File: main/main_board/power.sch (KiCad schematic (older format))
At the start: 28 parts, among them J1 Conn_02x08_Odd_Even, U3 MCP1755S-3302E/DB, U4 MCP1755S-3302E/DB, U7 MCP1755S-5002E/DB

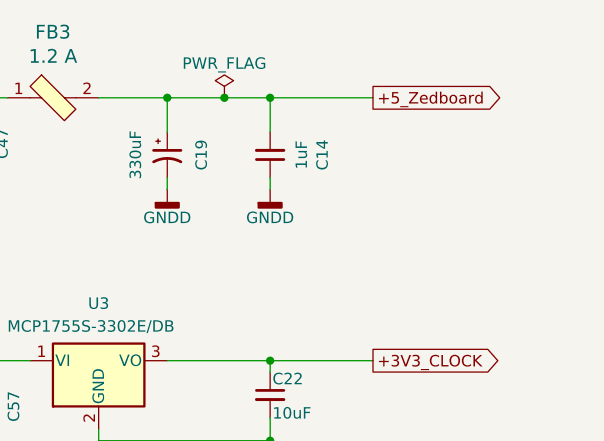
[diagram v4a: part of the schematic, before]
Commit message: Mostly work on main board layout. Aligned things on mm grid for easier routing, moved things around to create routing area. Neatened up component groups onto the grid. Parts of the routing plan are now drawn on the PCB.  See also notebook.txt. Reduced pad size of the PCIE connector, tweaked design rule clearances. Minor schematic tweaks.
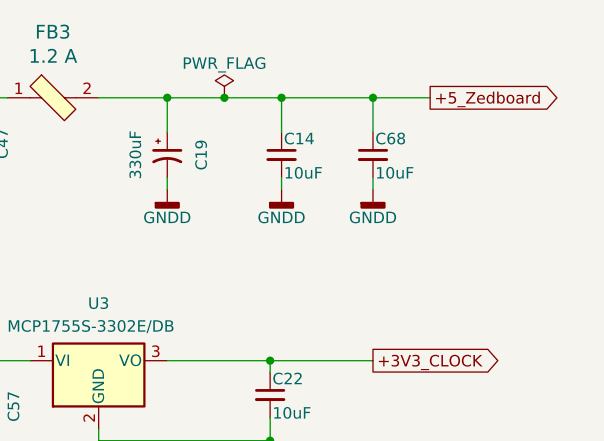
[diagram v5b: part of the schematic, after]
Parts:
- added C68: 10uF, Capacitor_SMD:C_0603_1608Metric, symbol Device:C_Small
- C14: value 1uF -> 10uF; footprint Capacitor_SMD:C_0805_2012Metric -> Capacitor_SMD:C_0603_1608Metric; DK line 27 -> 29; Description CAP CER 1UF 16V X7R 0805 -> CAP CER 10UF 6.3V X5R 0603; Digikey 1276-6471-1-ND -> 478-5318-1-ND; MPN CL21B105KOFNNNG -> 06036D106MAT2A; Manufacturer Samsung Electro-Mechanics -> (none)
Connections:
- net +5_Zedboard: now also C14.1, C68.1; no longer C14.2
- net GND: now also C14.2, C68.2; no longer C14.1
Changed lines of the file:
@@
 	1    0    0    -1
 $EndComp
-Text GLabel 9950 1200 2    50   Output ~ 0
+Text GLabel 10200 1200 2    50   Output ~ 0
 +5_Zedboard
 $Comp
@@
 $EndComp
 Wire Wire Line
-	9500 1200 9500 1350
-Wire Wire Line
-	9500 1550 9500 1600
+	9550 1200 9550 1350
+Wire Wire Line
+	9550 1550 9550 1600
 $Comp
 L power:GNDD #PWR011
 U 1 1 5ECF1209
-P 9500 1600
-F 0 "#PWR011" H 9500 1350 50  0001 C CNN
-F 1 "GNDD" H 9500 1475 50  0000 C CNN
-F 2 "" H 9500 1600 50  0001 C CNN
-F 3 "" H 9500 1600 50  0001 C CNN
-	1    9500 1600
-	1    0    0    -1
-$EndComp
-$Comp
-L Device:C_Small C?
-U 1 1 5ECEF1CE
-P 9500 1450
-AR Path="/5DFF6C0D/5ECEF1CE" Ref="C?"  Part="1"
-AR Path="/5E1D6729/5E1DA2AA/5ECEF1CE" Ref="C?"  Part="1"
-AR Path="/5E2EB92B/5ECEF1CE" Ref="C?"  Part="1"
-AR Path="/5E624B3C/5E2EB92B/5ECEF1CE" Ref="C?"  Part="1"
-AR Path="/5EBEDCCA/5ECEF1CE" Ref="C?"  Part="1"
-AR Path="/5E525EB8/5ECEF1CE" Ref="C?"  Part="1"
-AR Path="/5E525FC9/5ECEF1CE" Ref="C14"  Part="1"
-F 0 "C14" V 9271 1450 50  0000 C CNN
-F 1 "1uF" V 9362 1450 50  0000 C CNN
-F 2 "Capacitor_SMD:C_0805_2012Metric" H 9500 1450 50  0001 C CNN
-F 3 "https://media.digikey.com/pdf/Data%20Sheets/Samsung%20PDFs/CL_Series_MLCC_ds.pdf" H 9500 1450 50  0001 C CNN
-F 4 "CAP CER 1UF 16V X7R 0805 " H 9500 1450 50  0001 C CNN "Description"
-F 5 "1276-6471-1-ND" H 9500 1450 50  0001 C CNN "Digikey"
-F 6 "CL21B105KOFNNNG" H 9500 1450 50  0001 C CNN "MPN"
-F 7 "27" H 9500 1450 50  0001 C CNN "DK line"
-F 8 "Samsung Electro-Mechanics" H 9500 1450 50  0001 C CNN "Manufacturer"
-	1    9500 1450
-	-1   0    0    1
+P 9550 1600
+F 0 "#PWR011" H 9550 1350 50  0001 C CNN
+F 1 "GNDD" H 9550 1475 50  0000 C CNN
+F 2 "" H 9550 1600 50  0001 C CNN
+F 3 "" H 9550 1600 50  0001 C CNN
+	1    9550 1600
+	1    0    0    -1
 $EndComp
 Text GLabel 2250 1450 2    50   Output ~ 0
@@
 Text GLabel 3450 5050 2    50   Output ~ 0
 -6V
-Connection ~ 9500 1200
-Wire Wire Line
-	9500 1200 9950 1200
 Wire Wire Line
 	7900 1200 8100 1200
@@
 $EndComp
 Connection ~ 9300 1200
-Wire Wire Line
-	9300 1200 9500 1200
 $Comp
 L power:GNDD #PWR0108
@@
 	3950 2000 3950 2050
 Connection ~ 3950 2050
+$Comp
+L Device:C_Small C?
+U 1 1 5F0D2030
+P 9550 1450
+AR Path="/5DFCF14D/5DA78AA2/5F0D2030" Ref="C?"  Part="1"
+AR Path="/5DFCF14D/5E295469/5F0D2030" Ref="C?"  Part="1"
+AR Path="/5E448095/5DA78AA2/5F0D2030" Ref="C?"  Part="1"
+AR Path="/5E45936E/5DA78AA2/5F0D2030" Ref="C?"  Part="1"
+AR Path="/5E525F2C/5E6427A0/5DA78AA2/5F0D2030" Ref="C?"  Part="1"
+AR Path="/5E624B3C/5DFCF14D/5DA78AA2/5F0D2030" Ref="C?"  Part="1"
+AR Path="/5E624B3C/5E448095/5DA78AA2/5F0D2030" Ref="C?"  Part="1"
+AR Path="/5E624B3C/5E45936E/5DA78AA2/5F0D2030" Ref="C?"  Part="1"
+AR Path="/5E525F2C/5F0D2030" Ref="C?"  Part="1"
+AR Path="/5E525FC9/5F0D2030" Ref="C14"  Part="1"
+F 0 "C14" H 9560 1520 50  0000 L CNN
+F 1 "10uF" H 9560 1370 50  0000 L CNN
+F 2 "Capacitor_SMD:C_0603_1608Metric" H 9550 1450 50  0001 C CNN
+F 3 "http://datasheets.avx.com/cx5r.pdf" H 9550 1450 50  0001 C CNN
+F 4 "CAP CER 10UF 6.3V X5R 0603" H 9550 1450 50  0001 C CNN "Description"
+F 5 "478-5318-1-ND" H 9550 1450 50  0001 C CNN "Digikey"
+F 6 "06036D106MAT2A" H 9550 1450 50  0001 C CNN "MPN"
+F 7 "29" H 9550 1450 50  0001 C CNN "DK line"
+	1    9550 1450
+	1    0    0    -1
+$EndComp
+Wire Wire Line
+	9950 1550 9950 1600
+$Comp
+L power:GNDD #PWR0125
+U 1 1 5F0DBAD8
+P 9950 1600
+F 0 "#PWR0125" H 9950 1350 50  0001 C CNN
+F 1 "GNDD" H 9950 1475 50  0000 C CNN
+F 2 "" H 9950 1600 50  0001 C CNN
+F 3 "" H 9950 1600 50  0001 C CNN
+	1    9950 1600
+	1    0    0    -1
+$EndComp
+$Comp
+L Device:C_Small C?
+U 1 1 5F0DBAE2
+P 9950 1450
+AR Path="/5DFCF14D/5DA78AA2/5F0DBAE2" Ref="C?"  Part="1"
+AR Path="/5DFCF14D/5E295469/5F0DBAE2" Ref="C?"  Part="1"
+AR Path="/5E448095/5DA78AA2/5F0DBAE2" Ref="C?"  Part="1"
+AR Path="/5E45936E/5DA78AA2/5F0DBAE2" Ref="C?"  Part="1"
+AR Path="/5E525F2C/5E6427A0/5DA78AA2/5F0DBAE2" Ref="C?"  Part="1"
+AR Path="/5E624B3C/5DFCF14D/5DA78AA2/5F0DBAE2" Ref="C?"  Part="1"
+AR Path="/5E624B3C/5E448095/5DA78AA2/5F0DBAE2" Ref="C?"  Part="1"
+AR Path="/5E624B3C/5E45936E/5DA78AA2/5F0DBAE2" Ref="C?"  Part="1"
+AR Path="/5E525F2C/5F0DBAE2" Ref="C?"  Part="1"
+AR Path="/5E525FC9/5F0DBAE2" Ref="C68"  Part="1"
+F 0 "C68" H 9960 1520 50  0000 L CNN
+F 1 "10uF" H 9960 1370 50  0000 L CNN
+F 2 "Capacitor_SMD:C_0603_1608Metric" H 9950 1450 50  0001 C CNN
+F 3 "http://datasheets.avx.com/cx5r.pdf" H 9950 1450 50  0001 C CNN
+F 4 "CAP CER 10UF 6.3V X5R 0603" H 9950 1450 50  0001 C CNN "Description"
+F 5 "478-5318-1-ND" H 9950 1450 50  0001 C CNN "Digikey"
+F 6 "06036D106MAT2A" H 9950 1450 50  0001 C CNN "MPN"
+F 7 "29" H 9950 1450 50  0001 C CNN "DK line"
+	1    9950 1450
+	1    0    0    -1
+$EndComp
+Connection ~ 9550 1200
+Wire Wire Line
+	9550 1200 9950 1200
+Wire Wire Line
+	9300 1200 9550 1200
+Wire Wire Line
+	9950 1350 9950 1200
+Connection ~ 9950 1200
+Wire Wire Line
+	9950 1200 10200 1200
 $EndSCHEMATC

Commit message: Various preparations for routing the main board. Cleaned up the BOM and reconciled it with the Digikey BOM, so lots of component attributes have changed. This involved pinning down some components which had been vague, especially ferrite beads and chip capacitors. 1uF capacitors have all been changed to 10uF. Changed CARDSEL lines to be buffered rather than filtered, since we had the unused buffers sitting there. Another pass on the Microzed pin mapping.  Brought out the DEBUG LVDS line, and tweaked orderings. Added RC filter and pullups on I2C and PROBE_CONFIG.  We might need level translators here to get >=3.3V Added mount holes for the low volt regulator daughtercard, and dimensioned the connector location.
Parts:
- C10, C11, C59: value 1uF -> 10uF 16V; DK line 27 -> 10; Description CAP CER 1UF 16V X7R 0805 -> CAP CER 10UF 16V X5R 0805; Digikey 1276-6471-1-ND -> 399-8012-1-ND; MPN CL21B105KOFNNNG -> C0805C106K4PACTU; Manufacturer (none) -> KEMET
- C12, C13, C19, C20, C21: DK line 19 -> 21
- C14, C22, C23, C60, C68: DK line 29 -> 20; Manufacturer (none) -> AVX
- C15, C16, C17, C18, C47, C57, C58: value 1uF -> 10uF; footprint Capacitor_SMD:C_0805_2012Metric -> Capacitor_SMD:C_0603_1608Metric; DK line 27 -> 20; Description CAP CER 1UF 16V X7R 0805 -> CAP CER 10UF 6.3V X5R 0603; Digikey 1276-6471-1-ND -> 478-5318-1-ND; MPN CL21B105KOFNNNG -> 06036D106MAT2A; Manufacturer (none) -> AVX
- C66: MPN (none) -> DNP; Manufacturer (none) -> DNP
- D1, D2: DK line 41 -> 22
- D3: DK line 40 -> 23
- FB3: value 1.2 A -> 300 Ohm; footprint Inductor_SMD:L_0805_2012Metric -> Capacitor_SMD:C_2220_5650Metric; DK line (none) -> 13; Description (none) -> FERRITE BEAD 300 OHM 2220 1LN; Digikey (none) -> 240-2430-1-ND; MPN (none) -> HI2220R301R-10; Manufacturer (none) -> Laird-Signal Integrity Products
- J1: value Conn_02x08_Odd_Even -> Power
- U3, U4: DK line 25 -> 28; MPN (none) -> MCP1755S-3302E/DB; Manufacturer (none) -> Microchip Technology
- U7: DK line 25 -> 9; Description IC REG LIN 3.3V 300MA SOT223-3 -> IC REG LINEAR 5V 300MA SOT223-3; Digikey MCP1755S-3302E/DB-ND -> MCP1755S-5002E/DB-ND; MPN (none) -> MCP1755S-5002E/DB; Manufacturer (none) -> Microchip Technology
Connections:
- net +10V: now also J1.11 (Pin_11); no longer J1.12 (Pin_12)
- net +5VANA: now also J1.9 (Pin_9); no longer J1.10 (Pin_10)
- net +5VDIG: now also J1.7 (Pin_7); no longer J1.8 (Pin_8)
- net +5_CLOCK_IN: now also J1.3 (Pin_3); no longer J1.4 (Pin_4)
- net +5_DRIVERS_IN: now also J1.5 (Pin_5); no longer J1.6 (Pin_6)
- net +5_Zedboard_IN: now also J1.1 (Pin_1); no longer J1.2 (Pin_2)
- net -6V: now also J1.13 (Pin_13); no longer J1.14 (Pin_14)
- net GND: now also J1.10 (Pin_10), J1.12 (Pin_12), J1.14 (Pin_14), J1.2 (Pin_2), J1.4 (Pin_4), J1.6 (Pin_6), J1.8 (Pin_8); no longer J1.1 (Pin_1), J1.11 (Pin_11), J1.13 (Pin_13), J1.3 (Pin_3), J1.5 (Pin_5), J1.7 (Pin_7), J1.9 (Pin_9)

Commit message: Added testpoints, debug IO port, LEDs, and clock output jack.
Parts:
- added TP12: -6V, TestPoint:TestPoint_Keystone_5000-5004_Miniature, symbol Connector:TestPoint
- added TP13: Earth, TestPoint:TestPoint_Keystone_5000-5004_Miniature, symbol Connector:TestPoint
- added TP14: +10V, TestPoint:TestPoint_Keystone_5000-5004_Miniature, symbol Connector:TestPoint
- added TP15, TP16, TP17: GND, input:TestPoint_THTPad_D5.0mm_Drill2.41mm, symbol Connector:TestPoint
- added TP18: +5VDIG, TestPoint:TestPoint_Keystone_5000-5004_Miniature, symbol Connector:TestPoint
- added TP19: +5VANA, TestPoint:TestPoint_Keystone_5000-5004_Miniature, symbol Connector:TestPoint
- added TP20: OVDD, TestPoint:TestPoint_Keystone_5000-5004_Miniature, symbol Connector:TestPoint
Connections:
- net +10V: now also TP14.1
- net +5VANA: now also TP19.1
- net +5VDIG: now also TP18.1
- net -6V: now also TP12.1
- net Earth: now also TP13.1
- net GND: now also TP15.1, TP16.1, TP17.1
- net OVDD: now also TP20.1
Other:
- moved on the sheet: C18, C21

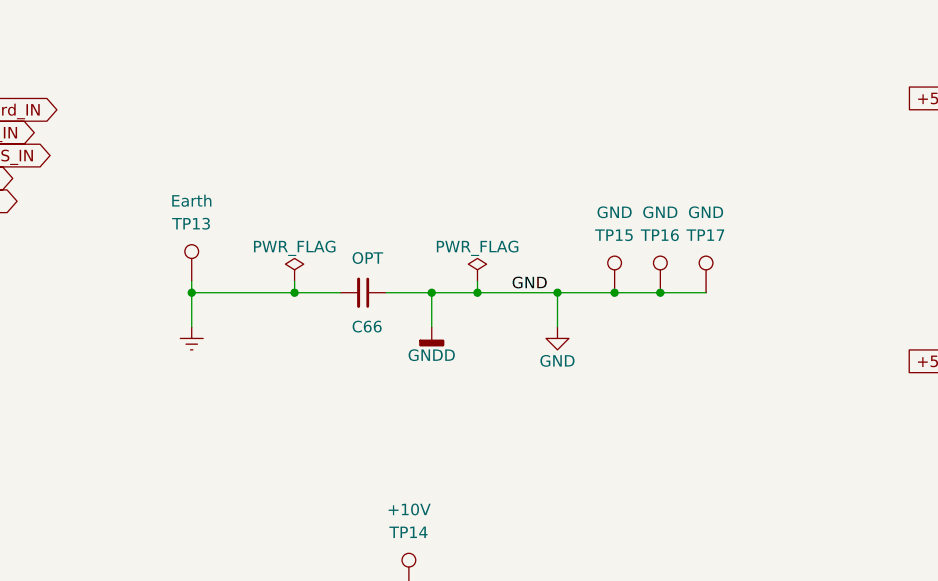
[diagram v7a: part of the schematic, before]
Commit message: Finishing up main/main_board/main_board.kicad_pcb.  Test points, stiching vias, ground pours.
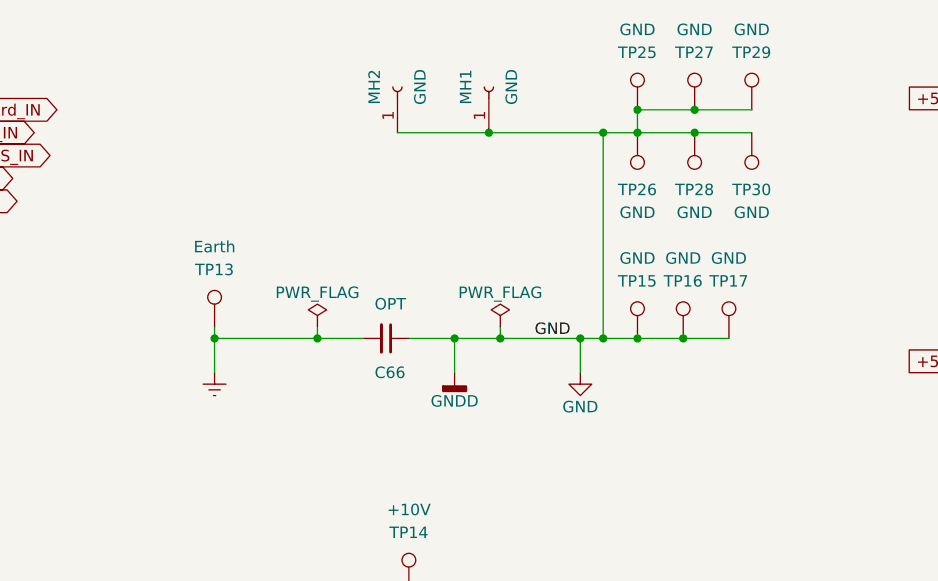
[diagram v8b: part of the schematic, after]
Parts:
- added MH1, MH2: GND, MountingHole:MountingHole_3.2mm_M3_Pad, symbol Connector:Conn_01x01_Female
- added TP25, TP26, TP27, TP28, TP29, TP30: GND, TestPoint:TestPoint_Keystone_5000-5004_Miniature, symbol Connector:TestPoint
- J1: DK line (none) -> 38; Description (none) -> Connector Header Through Hole 16 position 0.100\" (2.54mm); Digikey (none) -> SAM10854-ND; MPN (none) -> TSW-108-07-F-D; Manufacturer (none) -> Samtec Inc.
- TP15, TP16, TP17: DK line 33 -> 39
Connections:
- net GND: now also MH1.1 (Pin_1), MH2.1 (Pin_1), TP25.1, TP26.1, TP27.1, TP28.1, TP29.1, TP30.1
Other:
- moved on the sheet: C66, TP13, TP15, TP16, TP17
